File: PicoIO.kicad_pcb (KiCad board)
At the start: 2 copper layers, 73.2 x 58.4 mm, 35 parts, among them J1 Conn_01x03, J10 Conn_01x03, J11 Conn_01x03, J12 Conn_01x06, J13 Conn_01x03, J2 Conn_01x03, J3 Conn_01x03, J4 Conn_01x03, J5 Conn_01x03, J6 Conn_01x03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

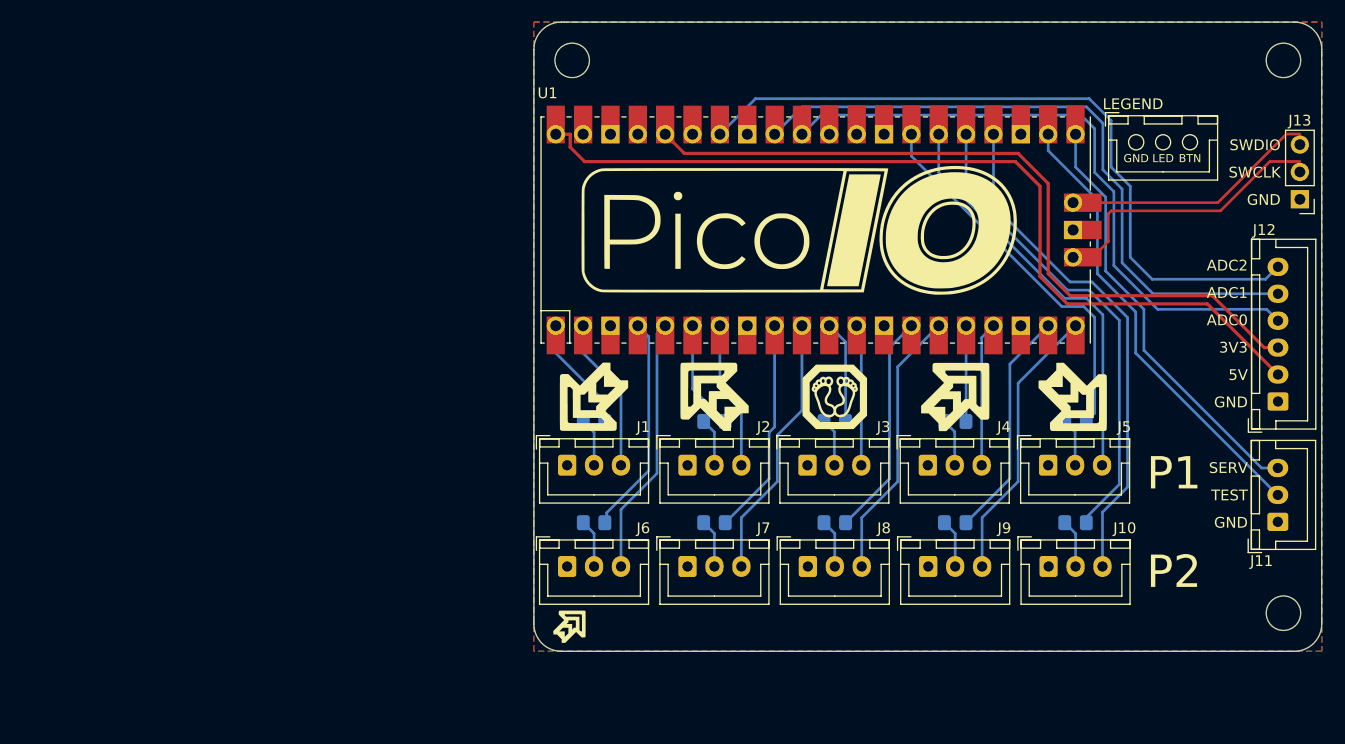
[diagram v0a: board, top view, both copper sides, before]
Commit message: Add MOSFETs, move to 4 pin JST, DRC passed
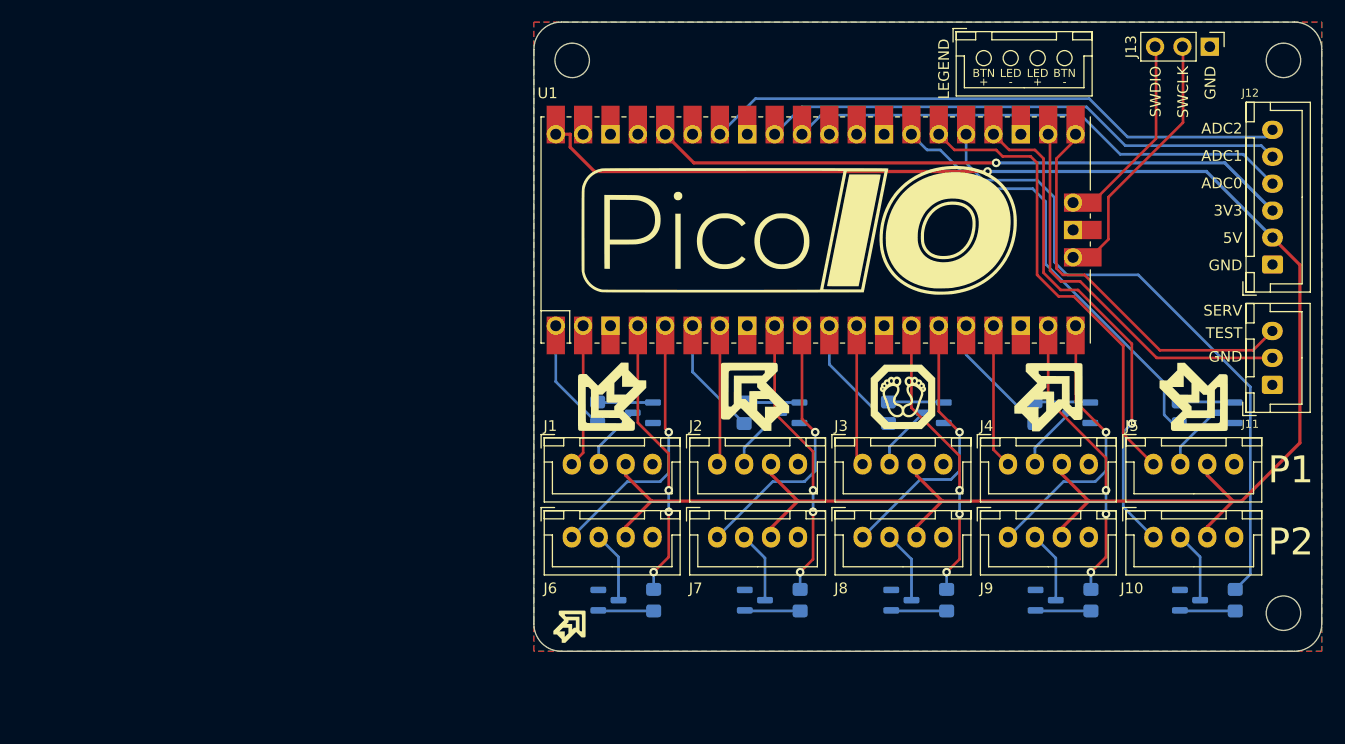
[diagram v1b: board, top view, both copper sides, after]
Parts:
- removed the J4 at (194.1, 100.1)
- removed the J5 at (213.4, 70.1)
- removed the J5 at (205.2, 100.1)
- added J4: Conn_01x04, Connector_JST:JST_XH_B4B-XH-A_1x04_P2.50mm_Vertical, F.Cu at (199.2, 62.3)
- added J4: Conn_01x04, Connector_JST:JST_XH_B4B-XH-A_1x04_P2.50mm_Vertical, F.Cu at (201.5, 100.0)
- added J5: Conn_01x04, Connector_JST:JST_XH_B4B-XH-A_1x04_P2.50mm_Vertical, F.Cu at (215.0, 100.0)
- added Q1: BSS138, Package_TO_SOT_SMD:SOT-23, B.Cu at (167.6, 95.2)
- added Q10: BSS138, Package_TO_SOT_SMD:SOT-23, B.Cu at (218.4, 112.6)
- added Q2: BSS138, Package_TO_SOT_SMD:SOT-23, B.Cu at (181.2, 95.2)
- added Q3: BSS138, Package_TO_SOT_SMD:SOT-23, B.Cu at (194.6, 95.2)
- added Q4: BSS138, Package_TO_SOT_SMD:SOT-23, B.Cu at (208.2, 95.2)
- added Q5: BSS138, Package_TO_SOT_SMD:SOT-23, B.Cu at (221.6, 95.2)
- added Q6: BSS138, Package_TO_SOT_SMD:SOT-23, B.Cu at (164.4, 112.6)
- added Q7: BSS138, Package_TO_SOT_SMD:SOT-23, B.Cu at (178.0, 112.6)
- added Q8: BSS138, Package_TO_SOT_SMD:SOT-23, B.Cu at (191.6, 112.6)
- added Q9: BSS138, Package_TO_SOT_SMD:SOT-23, B.Cu at (205.0, 112.6)
- J1, J10, J2, J3, J6, J7, J8, J9: value Conn_01x03 -> Conn_01x04; footprint Connector_JST:JST_XH_B3B-XH-A_1x03_P2.50mm_Vertical -> Connector_JST:JST_XH_B4B-XH-A_1x04_P2.50mm_Vertical
- R1, R10, R2, R3, R4, R5, R6, R7, R8, R9: value 330 -> 10K
- moved R10 16.5 mm to (222.6, 112.6), turned to -90 degrees
- moved J13 16.5 mm to (220.2, 61.2), turned to -90 degrees
- moved R9 14.5 mm to (209.2, 112.6), turned to -90 degrees
- moved J11 12.7 mm to (226.0, 92.6)
- moved J12 12.7 mm to (226.1, 81.4)
- moved R8 12.6 mm to (195.8, 112.6), turned to -90 degrees
- moved G*** 11.2 mm to (218.8, 93.7)
- moved R7 10.7 mm to (182.2, 112.6), turned to -90 degrees
- moved J10 10.1 mm to (215.0, 106.8)
- moved R5 9.66 mm to (217.4, 95.2), turned to 90 degrees
- moved R6 9.07 mm to (168.6, 112.6), turned to -90 degrees
- moved G*** 8.65 mm to (205.2, 93.8)
- moved J9 7.89 mm to (201.5, 106.8)
- moved R4 7.45 mm to (204.0, 95.2), turned to 90 degrees
- moved G*** 6.33 mm to (191.8, 93.7)
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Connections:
- J1 pad 1: GND -> P1 DL
- J1 pad 3: P1 DL -> +5V
- J10 pad 1: GND -> P2 DR
- J10 pad 3: P2 DR -> +5V
- J2 pad 1: GND -> P1 UL
- J2 pad 3: P1 UL -> +5V
- J3 pad 1: GND -> P1 CN
- J3 pad 3: P1 CN -> +5V
- J6 pad 1: GND -> P2 DL
- J6 pad 3: P2 DL -> +5V
- J7 pad 1: GND -> P2 UL
- J7 pad 3: P2 UL -> +5V
- J8 pad 1: GND -> P2 CN
- J8 pad 3: P2 CN -> +5V
- J9 pad 1: GND -> P2 UR
- J9 pad 3: P2 UR -> +5V
- R1 pad 2: Net-(J1-Pad2) -> Net-(Q1-Pad1)
- R10 pad 2: Net-(J10-Pad2) -> Net-(Q10-Pad1)
- R2 pad 2: Net-(J2-Pad2) -> Net-(Q2-Pad1)
- R3 pad 2: Net-(J3-Pad2) -> Net-(Q3-Pad1)
- R6 pad 2: Net-(J6-Pad2) -> Net-(Q6-Pad1)
- R7 pad 2: Net-(J7-Pad2) -> Net-(Q7-Pad1)
- R8 pad 2: Net-(J8-Pad2) -> Net-(Q8-Pad1)
- R9 pad 2: Net-(J9-Pad2) -> Net-(Q9-Pad1)
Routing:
- net +5V: track 81.9 -> 197.8 mm, vias 0 -> 1
- net P2 DR LED: track 44.4 -> 60.6 mm
- net ADC2: track 67.0 -> 54.4 mm
- net ADC1: track 61.5 -> 49.2 mm
- net ADC0: track 59.2 -> 47.1 mm
- net +3V3: track 70.0 -> 59.3 mm, vias 0 -> 1
- net P2 UL LED: track 20.2 -> 26.5 mm, vias 0 -> 3
- net Net-(J4-Pad2): track 0.00 -> 6.13 mm
- net Net-(J5-Pad2): track 0.00 -> 6.08 mm
- net P2 CN LED: track 20.8 -> 26.8 mm, vias 0 -> 3
- net P1 DR LED: track 35.2 -> 41.1 mm
- net P2 DL LED: track 20.4 -> 26.2 mm, vias 0 -> 3
- net P2 UR LED: track 21.5 -> 27.3 mm, vias 0 -> 3
- net TEST: track 42.3 -> 36.7 mm
- net P1 DR: track 38.3 -> 43.5 mm
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
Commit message: External LED power, some routing/aesthetic changes
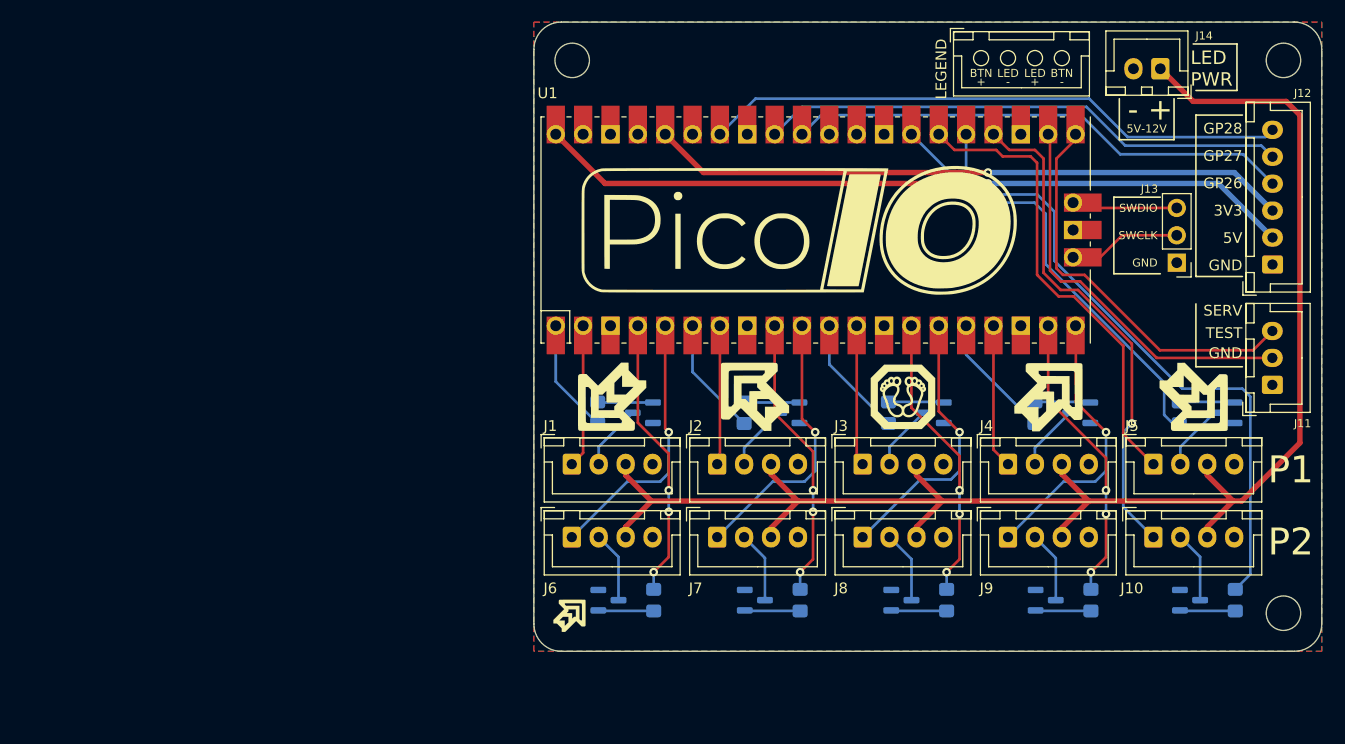
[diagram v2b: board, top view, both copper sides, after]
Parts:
- added G***: LOGO, LogoFootprints:InfinitesimalLoop_18mm, B.Cu at (169.9, 76.2)
- added G***: LOGO, LogoFootprints:InfinitesimalLogo_18mm, B.Cu at (169.9, 82.8)
- added J14: Conn_01x02, Connector_JST:JST_XH_B2B-XH-A_1x02_P2.50mm_Vertical, F.Cu at (215.6, 63.3)
- moved J13 20.3 mm to (217.2, 81.3), turned to 180 degrees
- moved G*** 1.02 mm to (160.8, 114.0)
- moved J4 0.25 mm to (199.0, 62.3)
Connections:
- net ADC0 renamed GP26
- net ADC1 renamed GP27
- net ADC2 renamed GP28
- J1 pad 3: +5V -> LED +
- J10 pad 3: +5V -> LED +
- J2 pad 3: +5V -> LED +
- J3 pad 3: +5V -> LED +
- J4 pad 3: +5V -> LED +
- J5 pad 3: +5V -> LED +
- J6 pad 3: +5V -> LED +
- J7 pad 3: +5V -> LED +
- J8 pad 3: +5V -> LED +
- J9 pad 3: +5V -> LED +
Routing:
- net LED +: track 0.00 -> 151.6 mm
- net +5V: track 197.8 -> 70.5 mm
- net SWCLK: track 24.8 -> 10.5 mm
- net SWDIO: track 18.7 -> 9.83 mm
- net P1 DR LED: track 41.1 -> 40.5 mm
- net P2 DR LED: track 60.6 -> 59.9 mm
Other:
- board text added: "+"
- board text added: "-"
- board text added: "5V-12V"
- board text added: "GP26"
- board text added: "GP27"
- board text added: "GP28"
- board text added: "LED PWR"
- board text added: "Try Infinitesimal!"
- board text added: "https://github.com/dj505/Infinitesimal"
- board text removed: "ADC0"
- board text removed: "ADC1"
- board text removed: "ADC2"

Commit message: Add buttonboard icons to PCB, generate gerber
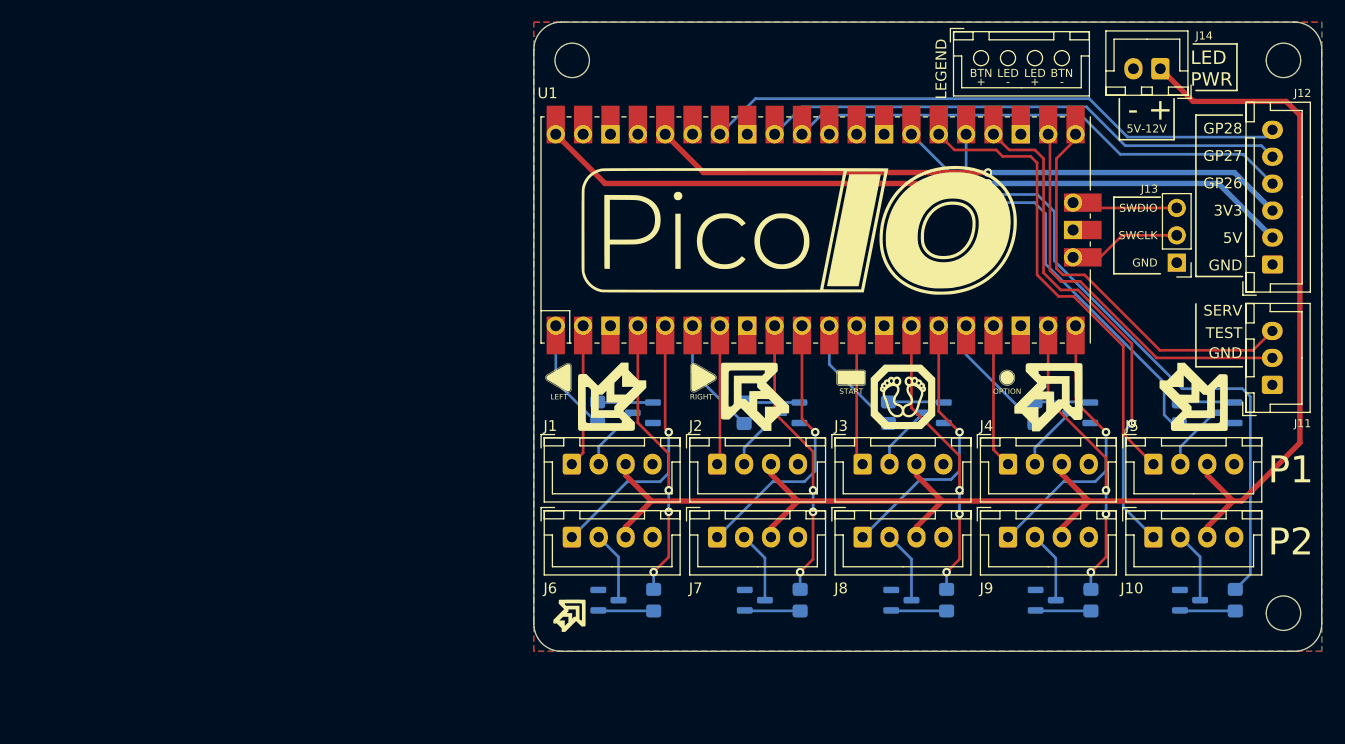
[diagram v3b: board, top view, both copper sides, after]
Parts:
- added G***: LOGO, LogoFootprints:Btnboard_Arrow-2_8mm, F.Cu at (159.8, 91.9)
- added G***: LOGO, LogoFootprints:Btnboard_Start-2_8mm, F.Cu at (186.9, 91.9)
- added G***: LOGO, LogoFootprints:Btnboard_Options-2_8mm, F.Cu at (201.4, 91.9)
- added G***: LOGO, LogoFootprints:Btnboard_Arrow-2_8mm, F.Cu at (173.2, 91.9)
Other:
- board text added: "LEFT"
- board text added: "OPTION"
- board text added: "RIGHT"
- board text added: "START"

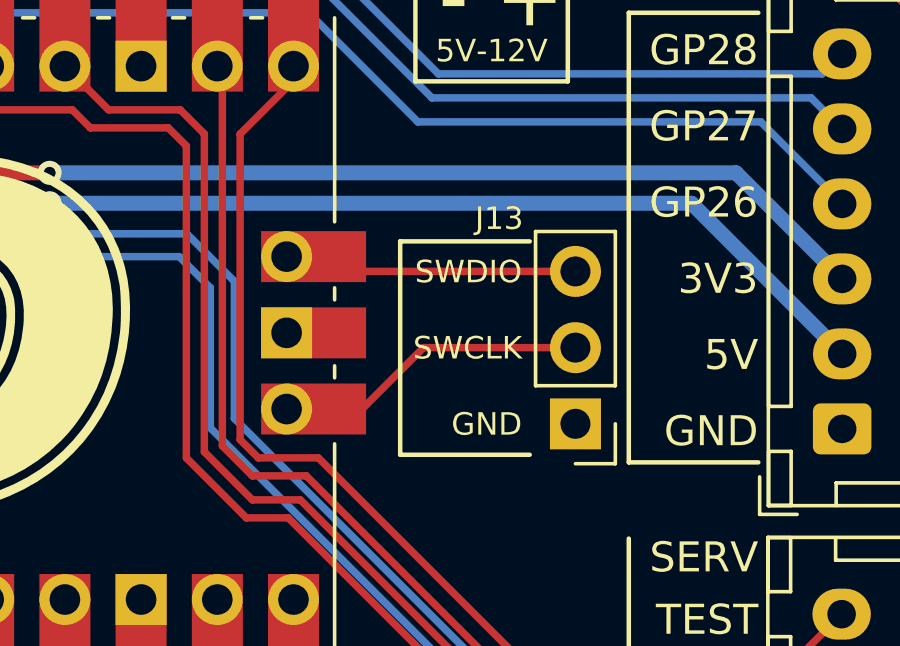
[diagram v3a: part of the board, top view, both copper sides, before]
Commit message: Extremely minor alignment nitpick
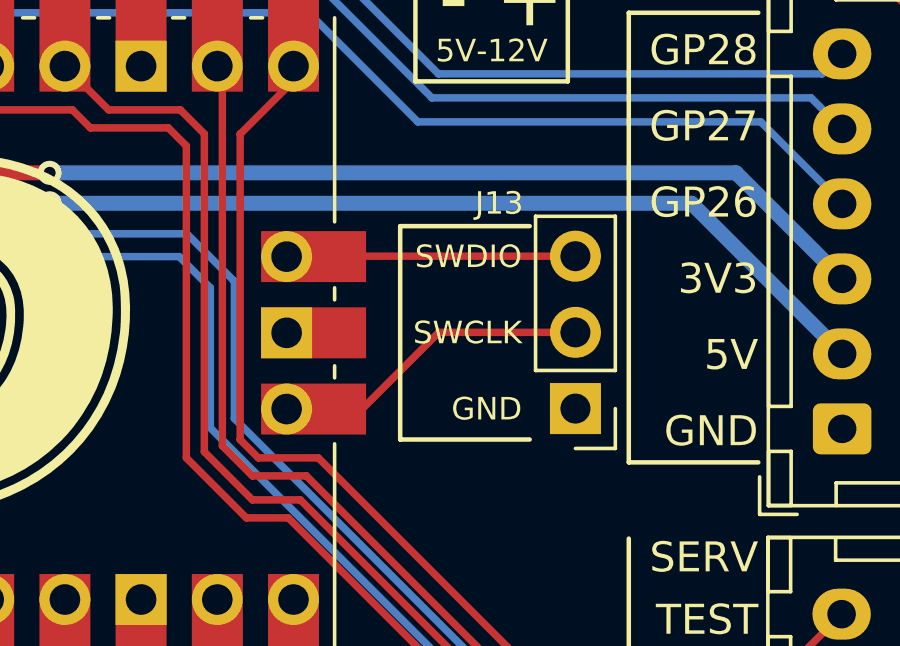
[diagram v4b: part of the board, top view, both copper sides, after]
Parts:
- moved J13 0.51 mm to (217.2, 80.8)
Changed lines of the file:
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@@
   )
   (footprint "Connector_PinHeader_2.54mm:PinHeader_1x03_P2.54mm_Vertical" (layer "F.Cu")
-    (at 217.17 81.265 180)
+    (at 217.17 80.757 180)
     (descr "Through hole straight pin header, 1x03, 2.54mm pitch, single row")
     (tags "Through hole pin header THT 1x03 2.54mm single row")
@@
     )
   )
-  (gr_line (start 215.646 75.184) (end 211.328 75.184) (layer "F.SilkS") (width 0.15))
-  (gr_line (start 211.328 82.296) (end 215.646 82.296) (layer "F.SilkS") (width 0.15))
+  (gr_line (start 215.646 74.676) (end 211.328 74.676) (layer "F.SilkS") (width 0.15))
+  (gr_line (start 211.328 81.788) (end 215.646 81.788) (layer "F.SilkS") (width 0.15))
   (gr_line (start 218.948 67.564) (end 218.948 82.55) (layer "F.SilkS") (width 0.15))
-  (gr_line (start 211.328 75.184) (end 211.328 82.296) (layer "F.SilkS") (width 0.15))
+  (gr_line (start 211.328 74.676) (end 211.328 81.788) (layer "F.SilkS") (width 0.15))
   (gr_line (start 218.948 90.932) (end 218.948 85.09) (layer "F.SilkS") (width 0.15))
   (gr_line (start 222.758 65.278) (end 218.948 65.278) (layer "F.SilkS") (width 0.15))
@@
     (effects (font (size 1 1) (thickness 0.15)))
   )
-  (gr_text "GND" (at 215.392 81.28) (layer "F.SilkS")
+  (gr_text "GND" (at 215.392 80.772) (layer "F.SilkS")
     (effects (font (size 0.75 0.75) (thickness 0.15)) (justify right))
   )
@@
     (effects (font (size 0.5 0.5) (thickness 0.125)) (justify left))
   )
-  (gr_text "SWDIO" (at 215.392 76.2) (layer "F.SilkS")
+  (gr_text "SWDIO" (at 215.392 75.692) (layer "F.SilkS")
     (effects (font (size 0.75 0.75) (thickness 0.15)) (justify right))
   )
@@
     (effects (font (size 1 1) (thickness 0.15)) (justify right))
   )
-  (gr_text "SWCLK\n" (at 215.392 78.74) (layer "F.SilkS")
+  (gr_text "SWCLK\n" (at 215.392 78.232) (layer "F.SilkS")
     (effects (font (size 0.75 0.75) (thickness 0.15)) (justify right))
   )
@@
   (segment (start 221.04 73.914) (end 226.06 78.934) (width 0.5) (layer "B.Cu") (net 25))
   (segment (start 199.644 73.914) (end 221.04 73.914) (width 0.5) (layer "B.Cu") (net 25))
-  (segment (start 210.058 80.772) (end 212.105 78.725) (width 0.25) (layer "F.Cu") (net 26))
-  (segment (start 212.105 78.725) (end 217.17 78.725) (width 0.25) (layer "F.Cu") (net 26))
   (segment (start 207.542 80.772) (end 210.058 80.772) (width 0.25) (layer "F.Cu") (net 26))
-  (segment (start 208.035 76.185) (end 217.17 76.185) (width 0.25) (layer "F.Cu") (net 27))
-  (segment (start 207.542 75.692) (end 208.035 76.185) (width 0.25) (layer "F.Cu") (net 27))
+  (segment (start 212.613 78.217) (end 217.17 78.217) (width 0.25) (layer "F.Cu") (net 26))
+  (segment (start 210.058 80.772) (end 212.613 78.217) (width 0.25) (layer "F.Cu") (net 26))
+  (segment (start 207.557 75.677) (end 217.17 75.677) (width 0.25) (layer "F.Cu") (net 27))
+  (segment (start 207.542 75.692) (end 207.557 75.677) (width 0.25) (layer "F.Cu") (net 27))
   (segment (start 163.5 98.3625) (end 163.5 99.975) (width 0.25) (layer "B.Cu") (net 32))
   (segment (start 166.6625 95.2) (end 163.5 98.3625) (width 0.25) (layer "B.Cu") (net 32))

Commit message: More small nitpicks
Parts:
- moved G*** 48.0 mm to (171.2, 100.3)
- moved G*** 48.0 mm to (144.2, 100.3)
- moved G*** 48.0 mm to (130.5, 100.3)
- moved G*** 48.0 mm to (157.7, 100.3)
- moved G*** 48.0 mm to (153.9, 98.5)
- moved G*** 48.0 mm to (125.7, 98.5)
- moved G*** 48.0 mm to (113.3, 120.6)
- moved J10 48.0 mm to (167.5, 113.3)
- moved J11 48.0 mm to (178.5, 99.1)
- moved J12 48.0 mm to (178.5, 88.0)
- moved J3 48.0 mm to (140.5, 106.5)
- moved J4 48.0 mm to (151.5, 68.8)
- moved J4 48.0 mm to (154.0, 106.5)
- moved J5 48.0 mm to (167.5, 106.5)
- moved J8 48.0 mm to (140.5, 113.3)
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
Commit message: Final logo placement, regenerate gerber files
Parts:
- added G***: LOGO, LogoFootprints:PicoIO-8_38mm, B.Cu at (144.0, 84.8)
- moved G*** 2.52 mm to (119.9, 82.7)
- moved G*** 2.52 mm to (119.9, 89.3)
